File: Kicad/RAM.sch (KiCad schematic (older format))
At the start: 6 parts, among them U32 74HCT157, U33 74HCT157, U34 74HCT157, U35 74HCT157, U36 HM62256BLP-7

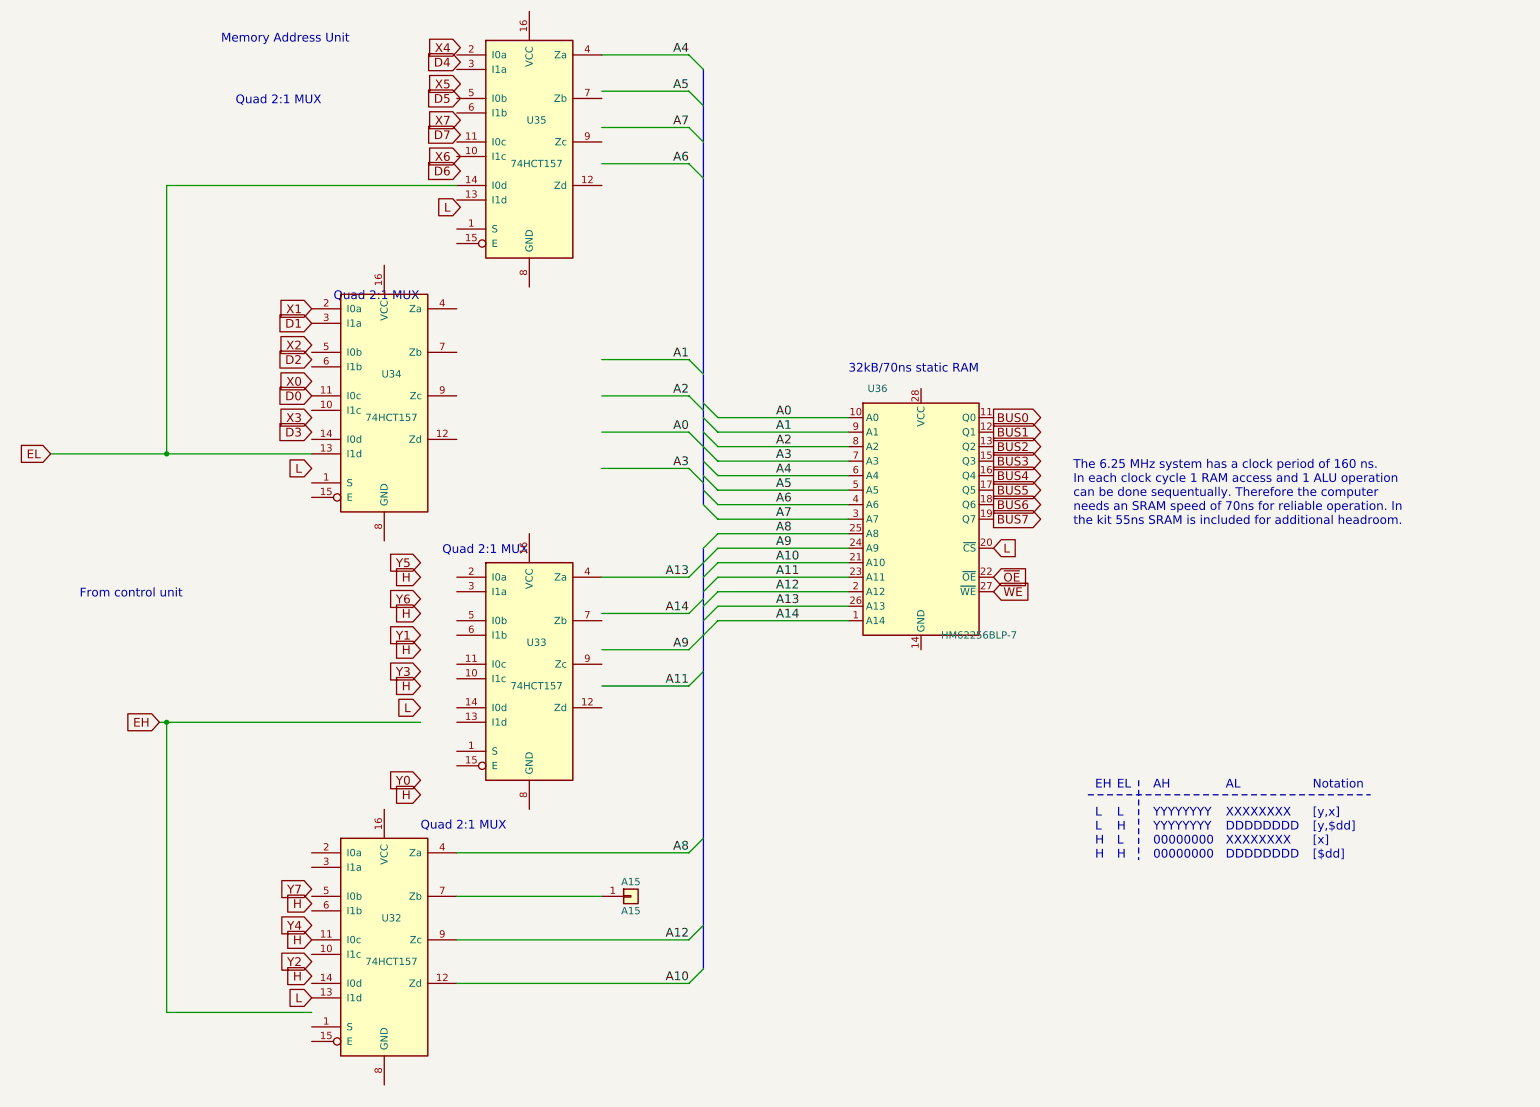
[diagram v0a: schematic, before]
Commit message: Update to work with mostly the default KiCAD items or items downloaded via the KiCAD Libraries too.
2 Resistors added of 1k on the lines for TRUE and FALSE pull ups.

Several things deleted which appeared at Graphic shapes on the PCB sometimes
but could not be edited. this was done manually at the bottom of the PCB_KiCAD file.

Deleted some PCB items around the order which marked the Copper limits of top and bottom. may have been tied to TRUE & FALSE.

Changed USB socket type.

This has been done not to change the board but to aid understanding and allow anyone who wants slightly easier access.

I have not tested it and provide no warranty.

Signed-off-by: John Bradley <flypie@rocketmail.com>
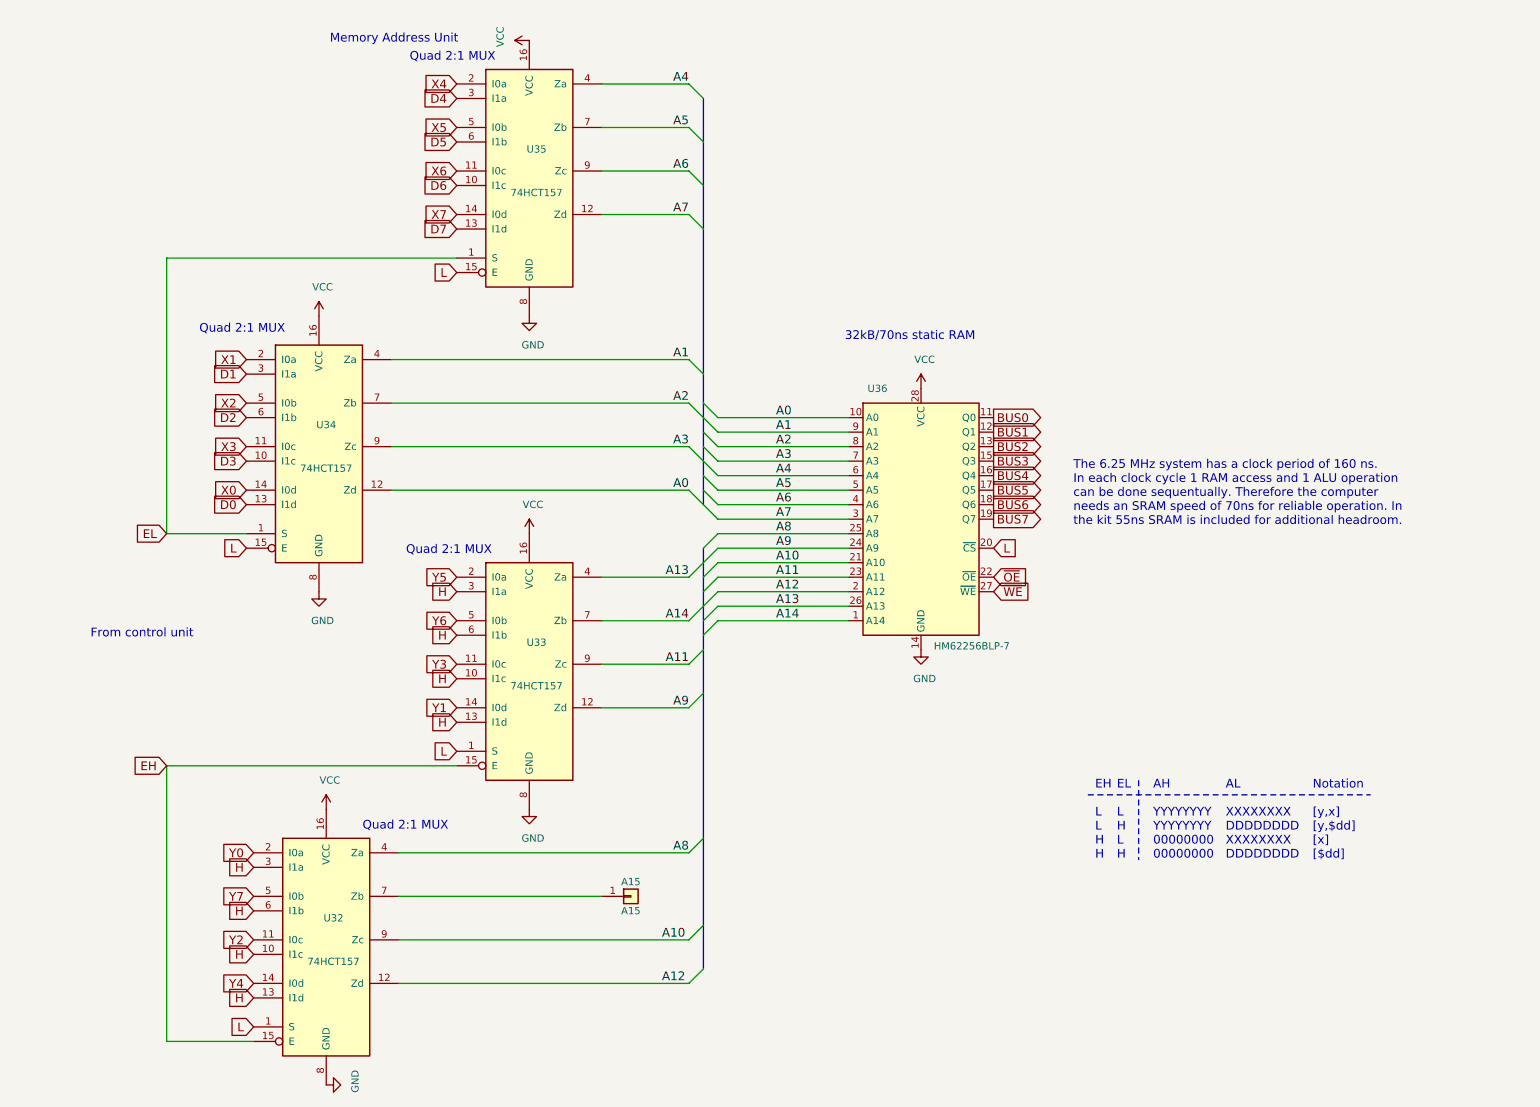
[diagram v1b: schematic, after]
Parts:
- A15: footprint Kicad:Breakout-1x1-MvK -> TestPoint:TestPoint_THTPad_D2.0mm_Drill1.0mm
- U36: footprint Package_DIP:DIP-20_W7.62mm -> Package_DIP:DIP-28_W15.24mm
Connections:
- net labels added: GND, VCC
- wire segments 39 -> 37
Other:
- moved on the sheet: U32, U34, U35
